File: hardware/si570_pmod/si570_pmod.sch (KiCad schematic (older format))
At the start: 14 parts, among them J1 Conn_01x06_Top_Bottom, J2 Conn_Coaxial, J3 Conn_Coaxial, U1 Si570

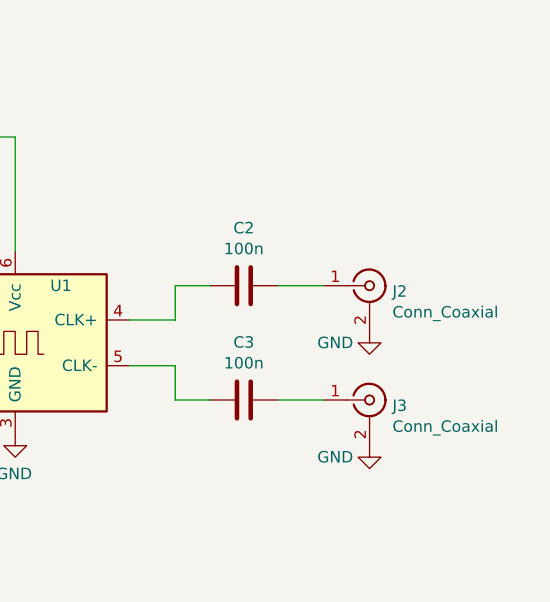
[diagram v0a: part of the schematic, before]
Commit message: fine-tune PCBs and FP, ordered first hardware
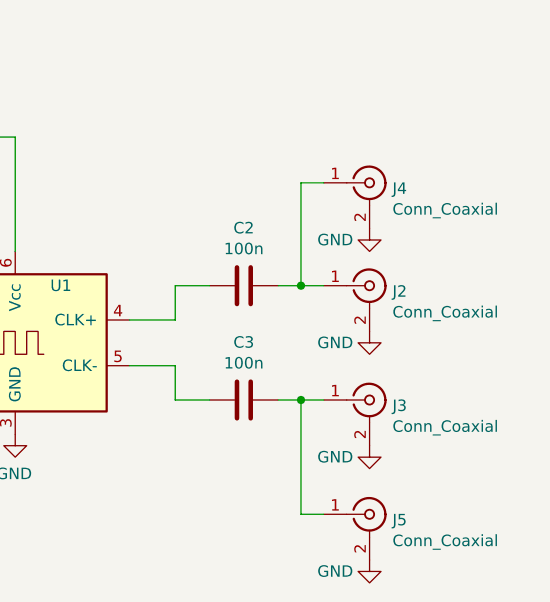
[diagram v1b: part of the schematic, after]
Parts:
- added J4, J5: Conn_Coaxial, Connector_Coaxial:SMA_Amphenol_132134-11_Vertical, symbol Connector:Conn_Coaxial
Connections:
- wire segments 33 -> 39
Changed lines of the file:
@@
 Wire Wire Line
 	5850 3400 6000 3400
-Wire Wire Line
-	6300 3400 6500 3400
 $Comp
 L Device:C C3
@@
 Wire Wire Line
 	5850 3900 6000 3900
-Wire Wire Line
-	6300 3900 6500 3900
 $Comp
 L Device:R R2
@@
 Wire Wire Line
 	4450 3950 4400 3950
+$Comp
+L Connector:Conn_Coaxial J4
+U 1 1 5DC1D44D
+P 6700 2950
+F 0 "J4" H 6800 2925 50  0000 L CNN
+F 1 "Conn_Coaxial" H 6800 2834 50  0000 L CNN
+F 2 "Connector_Coaxial:SMA_Amphenol_132134-11_Vertical" H 6700 2950 50  0001 C CNN
+F 3 " ~" H 6700 2950 50  0001 C CNN
+	1    6700 2950
+	1    0    0    -1
+$EndComp
+$Comp
+L Connector:Conn_Coaxial J5
+U 1 1 5DC1DFEE
+P 6700 4400
+F 0 "J5" H 6800 4375 50  0000 L CNN
+F 1 "Conn_Coaxial" H 6800 4284 50  0000 L CNN
+F 2 "Connector_Coaxial:SMA_Amphenol_132134-11_Vertical" H 6700 4400 50  0001 C CNN
+F 3 " ~" H 6700 4400 50  0001 C CNN
+	1    6700 4400
+	1    0    0    -1
+$EndComp
+$Comp
+L power:GND #PWR011
+U 1 1 5DC1E881
+P 6700 4600
+F 0 "#PWR011" H 6700 4350 50  0001 C CNN
+F 1 "GND" H 6850 4550 50  0000 C CNN
+F 2 "" H 6700 4600 50  0001 C CNN
+F 3 "" H 6700 4600 50  0001 C CNN
+	1    6700 4600
+	-1   0    0    -1
+$EndComp
+$Comp
+L power:GND #PWR010
+U 1 1 5DC1EF1D
+P 6700 3150
+F 0 "#PWR010" H 6700 2900 50  0001 C CNN
+F 1 "GND" H 6850 3100 50  0000 C CNN
+F 2 "" H 6700 3150 50  0001 C CNN
+F 3 "" H 6700 3150 50  0001 C CNN
+	1    6700 3150
+	-1   0    0    -1
+$EndComp
+Wire Wire Line
+	6300 3900 6400 3900
+Wire Wire Line
+	6300 3400 6400 3400
+Wire Wire Line
+	6400 3900 6400 4400
+Connection ~ 6400 3900
+Wire Wire Line
+	6400 3900 6500 3900
+Wire Wire Line
+	6400 4400 6500 4400
+Wire Wire Line
+	6400 2950 6400 3400
+Wire Wire Line
+	6400 2950 6500 2950
+Connection ~ 6400 3400
+Wire Wire Line
+	6400 3400 6500 3400
 $EndSCHEMATC
